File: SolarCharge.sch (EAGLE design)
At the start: 15 parts, among them U1 TINY4/5/9/10-TSHR/TS8R

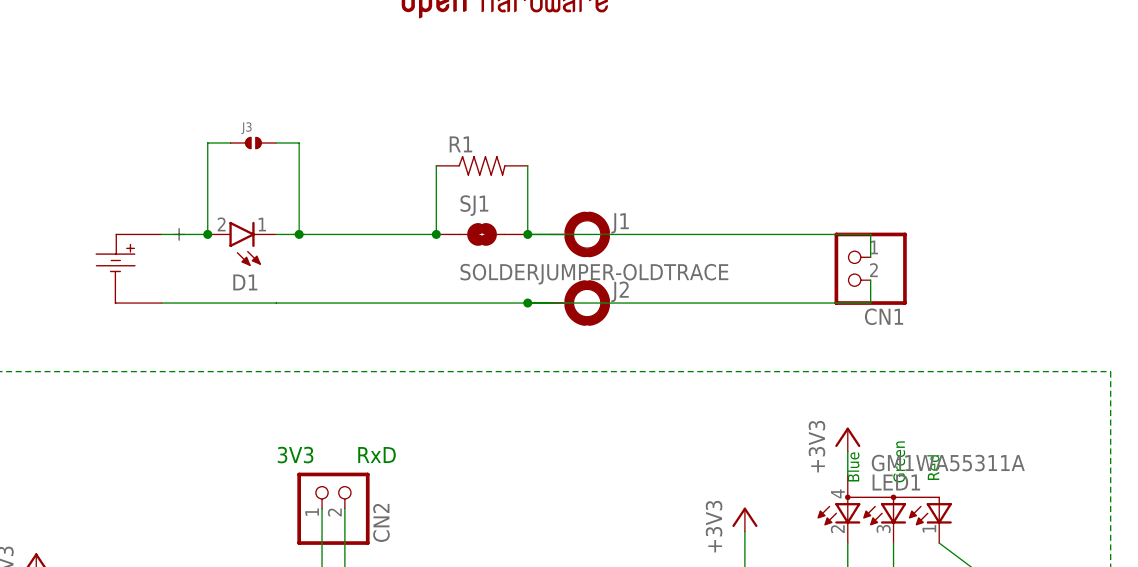
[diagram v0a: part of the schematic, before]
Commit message: Add second JST connector for solar out
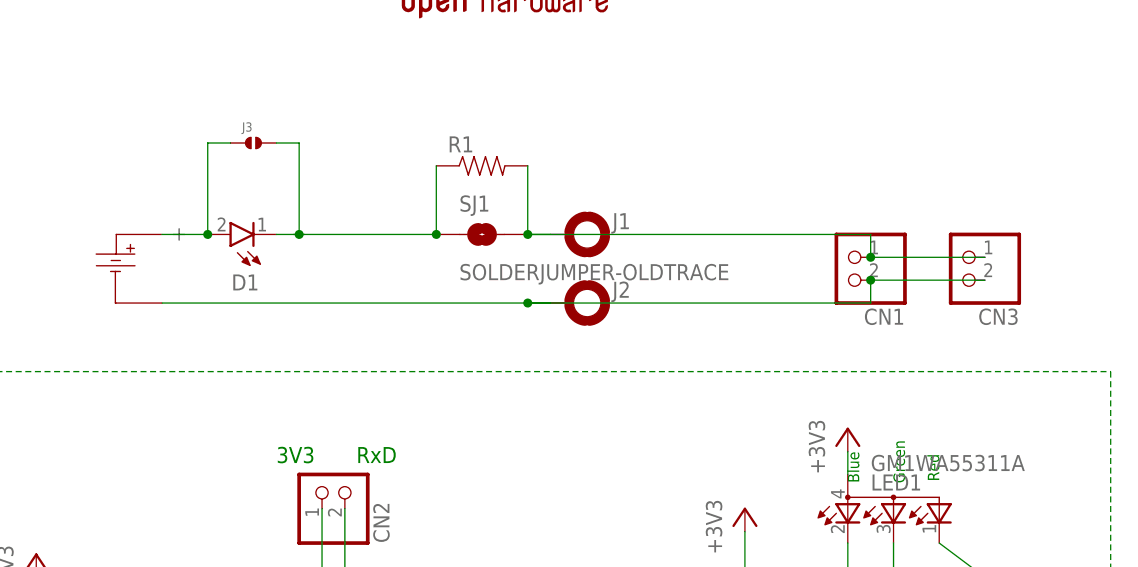
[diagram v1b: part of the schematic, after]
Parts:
- added CN3: (no value), lio:JST_2PIN-SMT-RA
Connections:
- net GND: now also CN3.1
- net N$4: now also CN3.2
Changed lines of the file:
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@@
 <setting verticaltext="up"/>
 </settings>
-<grid distance="0.05" unitdist="inch" unit="inch" style="lines" multiple="1" display="no" altdistance="0.01" altunitdist="inch" altunit="inch"/>
+<grid distance="0.1" unitdist="inch" unit="inch" style="lines" multiple="1" display="no" altdistance="0.01" altunitdist="inch" altunit="inch"/>
 <layers>
 <layer number="1" name="Top" color="4" fill="1" visible="no" active="no"/>
@@
 <part name="CN2" library="lio" deviceset="JST_2PIN" device="-SMT-RA"/>
 <part name="SJ2" library="SparkFun-Passives" deviceset="SOLDERJUMPER" device="NO"/>
+<part name="CN3" library="lio" deviceset="JST_2PIN" device="-SMT-RA"/>
 </parts>
 <sheets>
@@
 <instance part="CN2" gate="G$1" x="76.2" y="50.8" rot="MR90"/>
 <instance part="SJ2" gate="1" x="116.84" y="30.48"/>
+<instance part="CN3" gate="G$1" x="147.32" y="76.2" rot="R180"/>
 </instances>
 <busses>
@@
 <segment>
 <pinref part="U$1" gate="G$1" pin="P$2"/>
-<wire x1="58.42" y1="71.12" x2="71.12" y2="71.12" width="0.1524" layer="91"/>
 <pinref part="J2" gate="G$1" pin="MOUNT"/>
 <wire x1="101.6" y1="71.12" x2="99.06" y2="71.12" width="0.1524" layer="91"/>
 <pinref part="CN1" gate="G$1" pin="1"/>
-<wire x1="99.06" y1="71.12" x2="71.12" y2="71.12" width="0.1524" layer="91"/>
+<wire x1="99.06" y1="71.12" x2="58.42" y2="71.12" width="0.1524" layer="91"/>
 <wire x1="137.16" y1="73.66" x2="137.16" y2="71.12" width="0.1524" layer="91"/>
 <wire x1="137.16" y1="71.12" x2="99.06" y2="71.12" width="0.1524" layer="91"/>
 <junction x="99.06" y="71.12"/>
+<pinref part="CN3" gate="G$1" pin="1"/>
+<wire x1="149.86" y1="73.66" x2="137.16" y2="73.66" width="0.1524" layer="91"/>
+<junction x="137.16" y="73.66"/>
 </segment>
 <segment>
@@
 <wire x1="137.16" y1="76.2" x2="137.16" y2="78.74" width="0.1524" layer="91"/>
 <wire x1="137.16" y1="78.74" x2="99.06" y2="78.74" width="0.1524" layer="91"/>
-</segment>
-</net>
+<pinref part="CN3" gate="G$1" pin="2"/>
+<wire x1="149.86" y1="76.2" x2="137.16" y2="76.2" width="0.1524" layer="91"/>
+<junction x="137.16" y="76.2"/>
+</segment>
+</net>

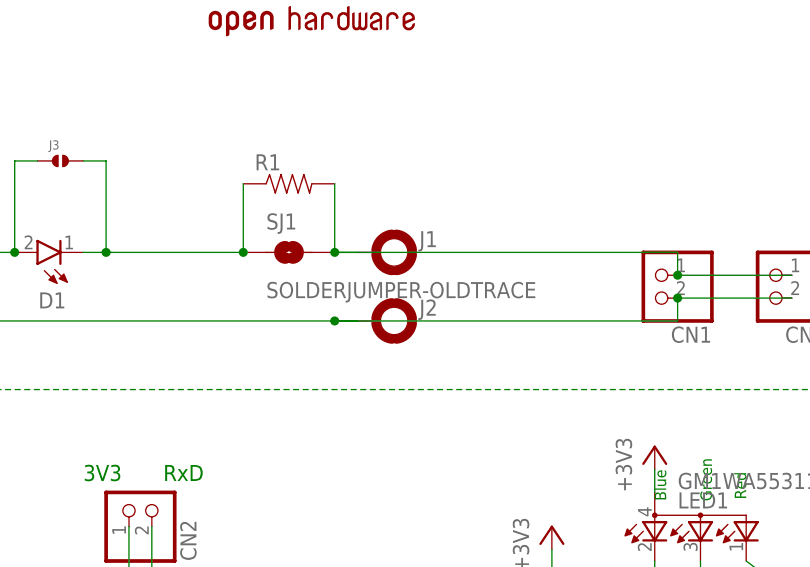
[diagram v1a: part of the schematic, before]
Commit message: Add Boost coverter to hookup Pi Zero W
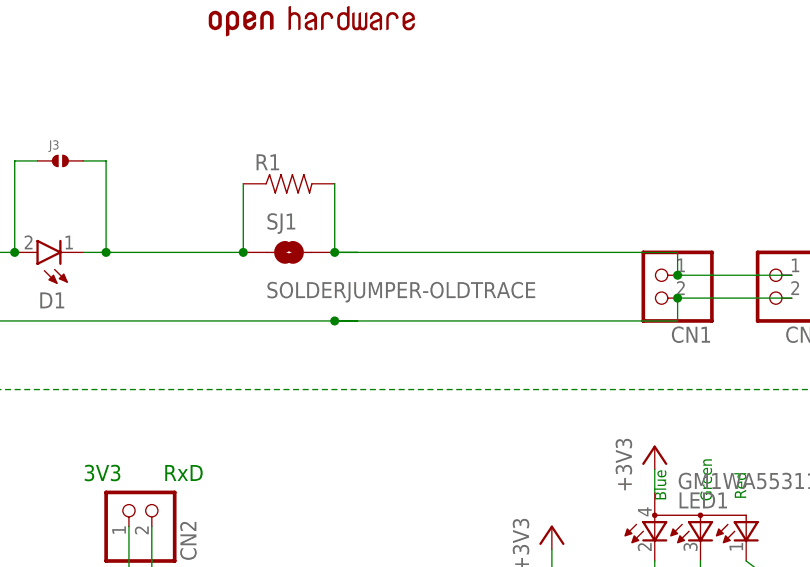
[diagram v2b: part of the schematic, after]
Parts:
- removed J1, J2: (no value), SparkFun-Connectors:STARBOARD_GND-WIDE
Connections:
- net GND: no longer J2.MOUNT
- net N$4: no longer J1.MOUNT
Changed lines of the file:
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@@
 <part name="D1" library="Wurth_Elektronik_Optoelectronics_rev15c" deviceset="WL-SWTP" device="3014"/>
 <part name="U$1" library="solar_panel_53_30" deviceset="SOLAR_CELL_53_30" device=""/>
-<part name="J1" library="SparkFun-Connectors" deviceset="STARBOARD_GND" device="-WIDE"/>
-<part name="J2" library="SparkFun-Connectors" deviceset="STARBOARD_GND" device="-WIDE"/>
 <part name="J3" library="solderjumper" deviceset="SOLDERJUMPER.2" device=".XL"/>
 <part name="R1" library="ROHM" deviceset="RESISTOR" device="0603-RES"/>
@@
 <instance part="D1" gate="G$1" x="68.58" y="78.74" rot="R180"/>
 <instance part="U$1" gate="G$1" x="53.34" y="71.12"/>
-<instance part="J1" gate="G$1" x="106.68" y="78.74"/>
-<instance part="J2" gate="G$1" x="106.68" y="71.12"/>
 <instance part="J3" gate="G$1" x="68.58" y="88.9"/>
 <instance part="R1" gate="G$1" x="93.98" y="86.36"/>
@@
 <segment>
 <pinref part="U$1" gate="G$1" pin="P$2"/>
-<pinref part="J2" gate="G$1" pin="MOUNT"/>
 <wire x1="101.6" y1="71.12" x2="99.06" y2="71.12" width="0.1524" layer="91"/>
 <pinref part="CN1" gate="G$1" pin="1"/>
@@
 <segment>
 <pinref part="SJ1" gate="1" pin="2"/>
-<pinref part="J1" gate="G$1" pin="MOUNT"/>
 <wire x1="99.06" y1="78.74" x2="101.6" y2="78.74" width="0.1524" layer="91"/>
 <pinref part="R1" gate="G$1" pin="2"/>

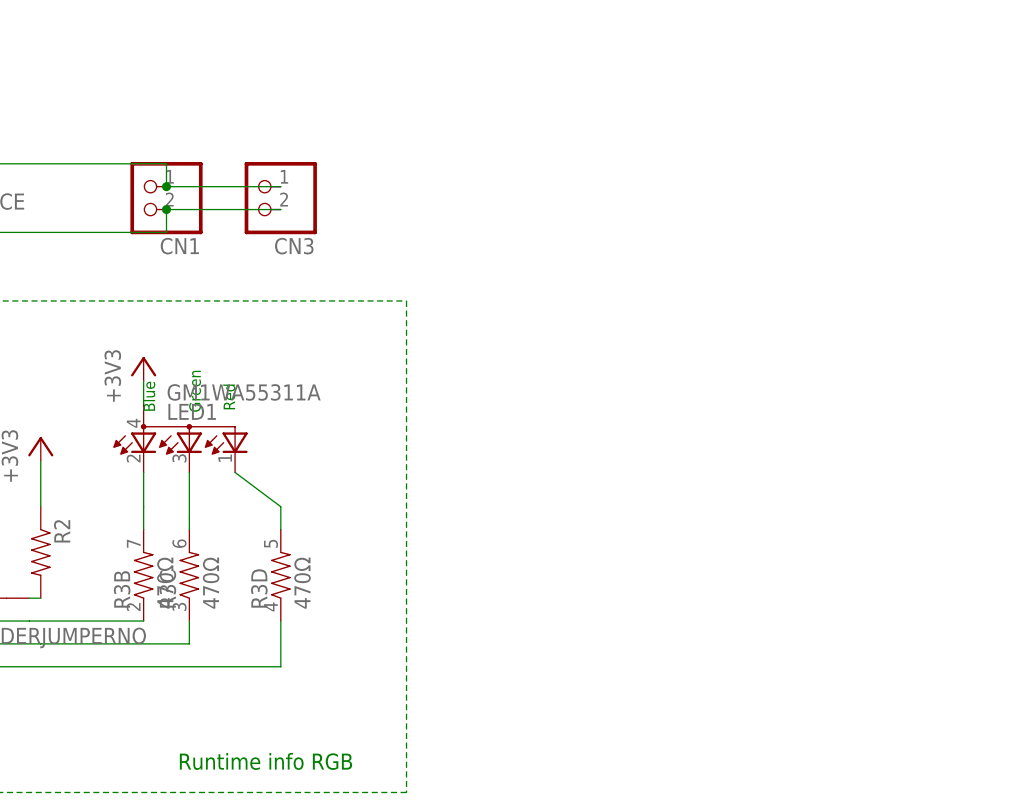
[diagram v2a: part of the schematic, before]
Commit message: Add p-channel mosfet for latching boost converter
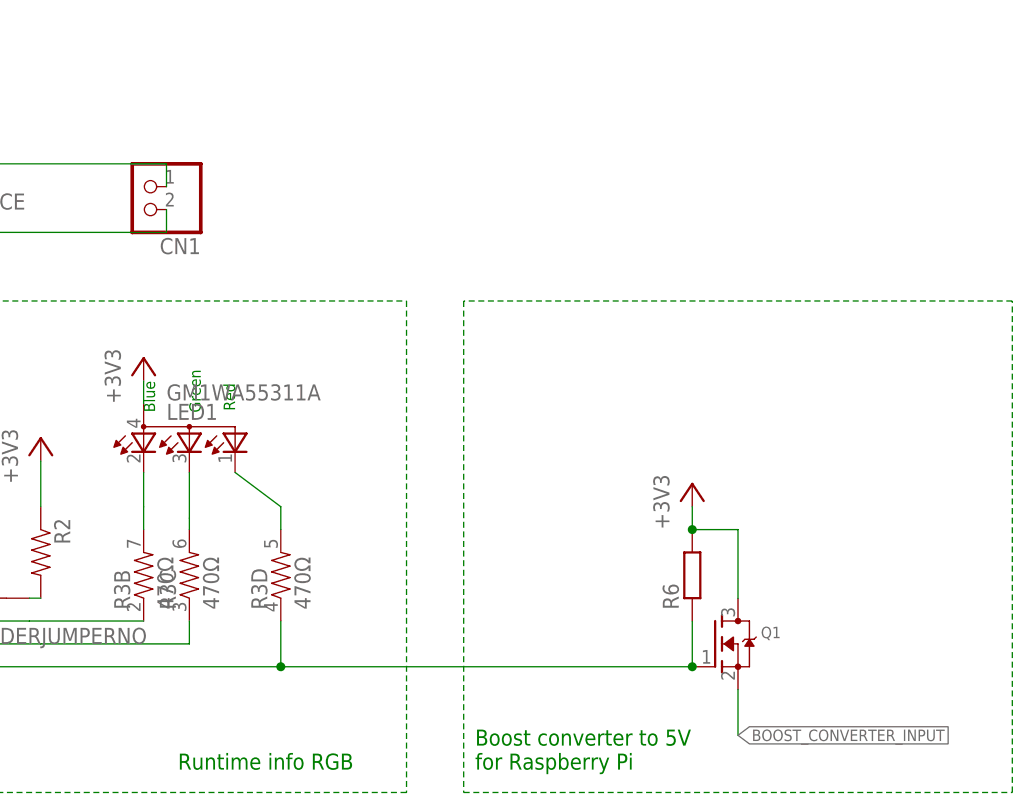
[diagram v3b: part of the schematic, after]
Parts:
- removed CN3: (no value), lio:JST_2PIN-SMT-RA
- added Q1: (no value), adafruit:MOSFET-NREFLOW
- added R6: (no value), rcl:R-EU_R0603
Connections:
- new net BOOST_CONVERTER_INPUT: Q1.S
- net +3V3: now also Q1.D, R6.2
- net GND: no longer CN3.1
- net N$4: no longer CN3.2
- net RED: now also Q1.G, R6.1
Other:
- note added: "Boost converter to 5V for Raspberry Pi"
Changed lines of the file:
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@@
 <setting verticaltext="up"/>
 </settings>
-<grid distance="0.1" unitdist="inch" unit="inch" style="lines" multiple="1" display="no" altdistance="0.01" altunitdist="inch" altunit="inch"/>
+<grid distance="0.05" unitdist="inch" unit="inch" style="lines" multiple="1" display="no" altdistance="0.01" altunitdist="inch" altunit="inch"/>
 <layers>
 <layer number="1" name="Top" color="4" fill="1" visible="no" active="no"/>
@@
 <part name="CN2" library="lio" deviceset="JST_2PIN" device="-SMT-RA"/>
 <part name="SJ2" library="SparkFun-Passives" deviceset="SOLDERJUMPER" device="NO"/>
-<part name="CN3" library="lio" deviceset="JST_2PIN" device="-SMT-RA"/>
+<part name="R6" library="rcl" deviceset="R-EU_" device="R0603"/>
+<part name="+3V13" library="supply1" deviceset="+3V3" device=""/>
+<part name="Q1" library="adafruit" deviceset="MOSFET-N" device="REFLOW"/>
 </parts>
 <sheets>
@@
 <text x="71.12" y="53.34" size="1.778" layer="91">3V3</text>
 <text x="138.43" y="11.43" size="1.778" layer="91">Runtime info RGB</text>
+<text x="171.45" y="11.43" size="1.778" layer="91">Boost converter to 5V
+for Raspberry Pi</text>
 </plain>
 <instances>
@@
 <instance part="CN2" gate="G$1" x="76.2" y="50.8" rot="MR90"/>
 <instance part="SJ2" gate="1" x="116.84" y="30.48"/>
-<instance part="CN3" gate="G$1" x="147.32" y="76.2" rot="R180"/>
+<instance part="R6" gate="G$1" x="195.58" y="33.02" rot="R90"/>
+<instance part="+3V13" gate="G$1" x="195.58" y="43.18"/>
+<instance part="Q1" gate="G$1" x="198.12" y="25.4"/>
 </instances>
 <busses>
@@
 <wire x1="137.16" y1="71.12" x2="99.06" y2="71.12" width="0.1524" layer="91"/>
 <junction x="99.06" y="71.12"/>
-<pinref part="CN3" gate="G$1" pin="1"/>
-<wire x1="149.86" y1="73.66" x2="137.16" y2="73.66" width="0.1524" layer="91"/>
-<junction x="137.16" y="73.66"/>
 </segment>
 <segment>
@@
 <wire x1="137.16" y1="76.2" x2="137.16" y2="78.74" width="0.1524" layer="91"/>
 <wire x1="137.16" y1="78.74" x2="99.06" y2="78.74" width="0.1524" layer="91"/>
-<pinref part="CN3" gate="G$1" pin="2"/>
-<wire x1="149.86" y1="76.2" x2="137.16" y2="76.2" width="0.1524" layer="91"/>
-<junction x="137.16" y="76.2"/>
 </segment>
 </net>
@@
 <wire x1="134.62" y1="52.07" x2="134.62" y2="54.61" width="0.1524" layer="91"/>
 </segment>
+<segment>
+<pinref part="R6" gate="G$1" pin="2"/>
+<pinref part="+3V13" gate="G$1" pin="+3V3"/>
+<wire x1="195.58" y1="40.64" x2="195.58" y2="38.1" width="0.1524" layer="91"/>
+<pinref part="Q1" gate="G$1" pin="D"/>
+<wire x1="200.66" y1="30.48" x2="200.66" y2="38.1" width="0.1524" layer="91"/>
+<wire x1="200.66" y1="38.1" x2="195.58" y2="38.1" width="0.1524" layer="91"/>
+<junction x="195.58" y="38.1"/>
+</segment>
 </net>
 <net name="RED_RESISTOR" class="0">
@@
 <wire x1="149.86" y1="27.94" x2="149.86" y2="22.86" width="0.1524" layer="91"/>
 <wire x1="149.86" y1="22.86" x2="110.49" y2="22.86" width="0.1524" layer="91"/>
+<pinref part="R6" gate="G$1" pin="1"/>
+<pinref part="Q1" gate="G$1" pin="G"/>
+<wire x1="195.58" y1="22.86" x2="195.58" y2="27.94" width="0.1524" layer="91"/>
+<wire x1="195.58" y1="22.86" x2="149.86" y2="22.86" width="0.1524" layer="91"/>
+<junction x="195.58" y="22.86"/>
+<junction x="149.86" y="22.86"/>
 </segment>
 </net>
@@
 </segment>
 </net>
+<net name="BOOST_CONVERTER_INPUT" class="0">
+<segment>
+<pinref part="Q1" gate="G$1" pin="S"/>
+<wire x1="200.66" y1="20.32" x2="200.66" y2="15.24" width="0.1524" layer="91"/>
+<label x="200.66" y="15.24" size="1.27" layer="95" xref="yes"/>
+</segment>
+</net>
+<net name="N$2" class="0">
+<segment>
+<wire x1="170.18" y1="63.5" x2="170.18" y2="8.89" width="0.1524" layer="91" style="shortdash"/>
+<wire x1="170.18" y1="8.89" x2="231.14" y2="8.89" width="0.1524" layer="91" style="shortdash"/>
+<wire x1="231.14" y1="8.89" x2="231.14" y2="63.5" width="0.1524" layer="91" style="shortdash"/>
+<wire x1="231.14" y1="63.5" x2="170.18" y2="63.5" width="0.1524" layer="91" style="shortdash"/>
+</segment>
+</net>
 </nets>
 </sheet>
@@
 </drawing>
 <compatibility>
+<note version="6.3" minversion="6.2.2" severity="warning">
+Since Version 6.2.2 text objects can contain more than one line,
+which will not be processed correctly with this version.
+</note>
 <note version="8.2" severity="warning">
 Since Version 8.2, EAGLE supports online libraries. The ids
